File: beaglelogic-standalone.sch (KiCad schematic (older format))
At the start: 238 parts, among them J1 USB_OTG, J2 USB_A, J3 CONN_01X06, J4 SI-51009-F, J5 CONN_02X12, J6 CONN_02X16, Q1 BSS138, Q2 BSS138, SW1 SW_PUSH_SMALL_H, SW2 SW_PUSH_SMALL_H, U1 AP1117, U10 MCP79410/TDFN, U11 SST26VF064B, U12 TPS73101, U13 SN74LVCH16T245, U14 DVIULC6-4SC6, U15 DVIULC6-4SC6, U16 DVIULC6-4SC6, U17 DVIULC6-4SC6, U18 74LV1T125, U19 74LVC1G06, U2 TPS2051C, U20 EMMC_4G, U3 74LVC1G07, U4 TPD4S012, U5 TPD4S012, U6 OSD3358, U7 KSZ9031RNXCC, U8 74LVC2G241, U9 24LC32AT-I/OT, Y1 25MHz, Y2 24MHz, Y3 32.768kHz,CL=9pF

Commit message: Fix connection to GND of C31
Was unconnected though appeared connected

Signed-off-by: Kumar Abhishek <abhishek@theembeddedkitchen.net>
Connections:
- net GND: now also C31.2
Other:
- note added: "Serial Debug"

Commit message: Attach GPIO_OE to its own GPIO instead of SYS_RESETn
Signed-off-by: Kumar Abhishek <abhishek@theembeddedkitchen.net>
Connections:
- net SYS_RESETn: no longer R46.1
- net GPIO_OE: now reaches U6.T16 (GPMC_A10)
- net GPIO_OE: now also R46.1

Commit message: Add jumpered buffer to CS line of SPI Flash
Suggested change by @mwelling to enable recovery from a board brick.

Signed-off-by: Kumar Abhishek <abhishek@theembeddedkitchen.net>
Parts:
- added JP?: SPIF_Enable, Measurement_Points:Test_Point_2Pads, symbol Jumper_NC_Small
- added R?: 10K, Resistors_SMD:R_0402, symbol R
- added R?: 100K, Resistors_SMD:R_0402, symbol R
- U19: value 74LVC1G06 -> 74LVC1G125; symbol 74LVC1G06 -> 74LVC1G125
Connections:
- net +3V3: now also R?.2, R?.2
- net EMMC_RSTn: no longer U19.4
- net GND: now also JP?.1
- net SPIF_CS: now also U19.2; no longer U11.1 (S#)
- net EMMC_RESET renamed EMMC_RESETn
- net EMMC_RESETn: no longer U19.2
- new net: JP?.2, R?.1, U19.1
- new net: R?.1, U11.1 (S#), U19.4
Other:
- moved on the sheet: BT1, C53, U19

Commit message: Insert series resistors on SPIF SCK, eMMC CLK and SD CLK
Signed-off-by: Kumar Abhishek <abhishek@theembeddedkitchen.net>
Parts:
- added R? (x3): 33R, Resistors_SMD:R_0402, symbol R
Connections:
- net EMMC_CLK: now also R?.1; no longer R77.1, U20.M6 (CLK)
- net MMC0_CLK: now also R?.1; no longer R54.1, SOK1.5 (CLK)
- net SPIF_SCK: now also R?.1; no longer U11.6 (C)
- new net: R54.1, R?.2, SOK1.5 (CLK)
- new net: R77.1, R?.2, U20.M6 (CLK)
- new net: R?.2, U11.6 (C)
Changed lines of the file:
@@
 Text Label 17950 1700 2    50   ~ 0
 MMC0_CMD
-Text Label 17950 1900 2    50   ~ 0
+Text Label 16450 2700 2    50   ~ 0
 MMC0_CLK
 Text Label 17700 2100 2    50   ~ 0
@@
 Text Label 20850 2400 2    50   ~ 0
 EMMC_CMD
-Text Label 20850 2500 2    50   ~ 0
+Text Label 19950 2850 2    50   ~ 0
 EMMC_CLK
 $Comp
@@
 	0    -1   -1   0
 $EndComp
-Text Label 13900 2400 2    50   ~ 0
+Text Label 13500 2200 0    50   ~ 0
 SPIF_SCK
 Text Label 13900 2300 2    50   ~ 0
@@
 	16900 5700 17000 5700
 Wire Wire Line
-	17000 5700 17000 8000
+	17000 8000 17000 5700
 Wire Wire Line
-	17000 8000 16950 8000
+	16900 8000 16950 8000
 Wire Wire Line
-	16950 8000 16900 8000
+	16950 8000 17000 8000
 Wire Wire Line
 	16900 6000 17100 6000
@@
 	17050 1400 17050 1900
 Wire Wire Line
+	17050 1900 17050 2700
+Wire Wire Line
 	16850 1400 16850 2100
 Wire Wire Line
@@
 	19700 1350 19700 2500
 Wire Wire Line
-	19700 2500 20900 2500
+	19700 2500 20450 2500
+Wire Wire Line
+	20450 2500 20900 2500
 Wire Wire Line
 	19600 1350 19600 2650
@@
 Connection ~ 12950 2450
 Wire Wire Line
-	12400 2450 12250 2450
-Wire Wire Line
-	12250 2450 12250 2450
+	12250 2450 12400 2450
 $Comp
 L GND #PWR?
@@
 	0    1    1    0
 $EndComp
+$Comp
+L R R?
+U 1 1 596EAD95
+P 16800 2700
+F 0 "R?" V 16750 2950 50  0000 R CNN
+F 1 "33R" V 16800 2800 50  0000 R CNN
+F 2 "Resistors_SMD:R_0402" V 16730 2700 50  0001 C CNN
+F 3 "" H 16800 2700 50  0001 C CNN
+	1    16800 2700
+	0    -1   1    0
+$EndComp
+Wire Wire Line
+	17050 2700 16950 2700
+Connection ~ 17050 1900
+Wire Wire Line
+	16450 2700 16650 2700
+$Comp
+L R R?
+U 1 1 596ECB19
+P 20250 2850
+F 0 "R?" V 20200 3100 50  0000 R CNN
+F 1 "33R" V 20250 2950 50  0000 R CNN
+F 2 "Resistors_SMD:R_0402" V 20180 2850 50  0001 C CNN
+F 3 "" H 20250 2850 50  0001 C CNN
+	1    20250 2850
+	0    -1   1    0
+$EndComp
+Wire Wire Line
+	20400 2850 20450 2850
+Wire Wire Line
+	20450 2850 20450 2500
+Connection ~ 20450 2500
+Wire Wire Line
+	19950 2850 20100 2850
+$Comp
+L R R?
+U 1 1 596F921B
+P 13750 2400
+F 0 "R?" V 13700 2650 50  0000 R CNN
+F 1 "33R" V 13750 2500 50  0000 R CNN
+F 2 "Resistors_SMD:R_0402" V 13680 2400 50  0001 C CNN
+F 3 "" H 13750 2400 50  0001 C CNN
+	1    13750 2400
+	0    -1   1    0
+$EndComp
+Wire Wire Line
+	13600 2400 13450 2400
+Wire Wire Line
+	13450 2400 13450 2200
+Wire Wire Line
+	13450 2200 13500 2200
 $EndSCHEMATC

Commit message: Update to Revision A2
Signed-off-by: Kumar Abhishek <abhishek@theembeddedkitchen.net>
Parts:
- gave numbers to parts that had none: 6
- renumbered C53 to C37, C37 to C38, C38 to C39, C39 to C40, C40 to C41, C41 to C42, C42 to C43, C43 to C44, C44 to C45, C45 to C46, C46 to C47, C47 to C48, C48 to C49, C49 to C50, C50 to C51, C51 to C52, C52 to C53, R95 to R100, R96 to R101, R97 to R102, R98 to R103, R99 to R104, R100 to R105, R101 to R106, R102 to R107, R103 to R108, R104 to R109, R105 to R110, R106 to R111, R107 to R112, R108 to R113, R109 to R114, R110 to R115, R111 to R116, R112 to R117, R113 to R118, R114 to R119, R115 to R120, R116 to R121, R117 to R122, R118 to R123, R119 to R124, R42 to R45, R43 to R46, R44 to R47, R45 to R48, R46 to R49, R47 to R50, R48 to R51, R49 to R52, R50 to R53, R51 to R55, R52 to R56, R53 to R57, R54 to R58, R55 to R59, R56 to R60, R57 to R61, R58 to R62, R59 to R63, R60 to R64, R61 to R65, R62 to R66, R63 to R67, R64 to R68, R65 to R69, R66 to R70, R67 to R71, R68 to R72, R69 to R73, R70 to R74, R71 to R75, R72 to R76, R73 to R77, R74 to R78, R75 to R79, R76 to R80, R77 to R81, R78 to R82, R79 to R83, R80 to R84, R81 to R85, R82 to R86, R83 to R87, R84 to R88, R85 to R89, R86 to R90, R87 to R91, R88 to R92, R89 to R93, R90 to R94, R91 to R95, R92 to R97, R93 to R98, R94 to R99, U19 to U10, U10 to U11, U11 to U12, U12 to U13, U13 to U14, U14 to U15, U15 to U16, U16 to U17, U17 to U18, U18 to U19

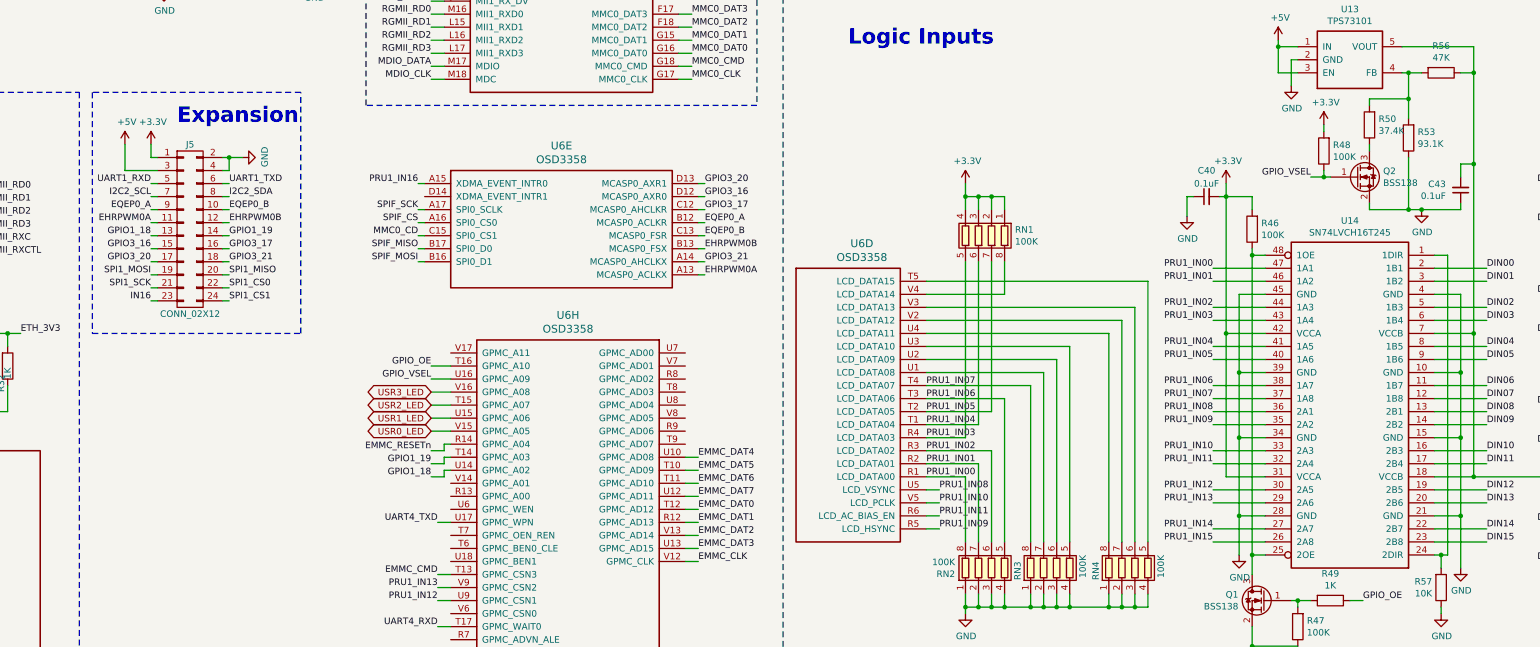
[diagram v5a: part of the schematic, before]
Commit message: Add pull-ups on I2C2 lines
Signed-off-by: Kumar Abhishek <abhishek@theembeddedkitchen.net>
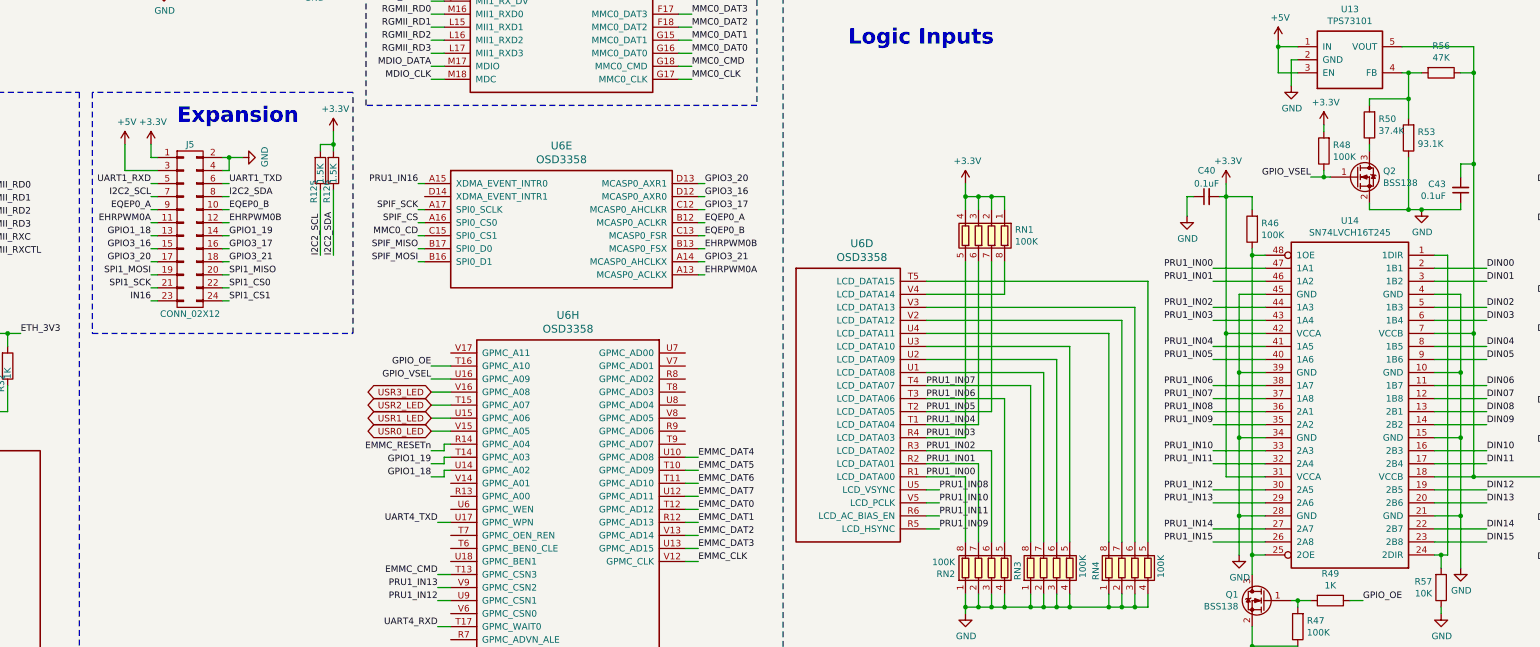
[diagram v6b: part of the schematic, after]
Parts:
- added R125, R126: 1.5K, Resistors_SMD:R_0402, symbol R
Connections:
- net +3V3: now also R125.2, R126.2
- net I2C2_SCL: now also R125.1
- net I2C2_SDA: now also R126.1

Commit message: Replace OSD3358 with OSD3358-SM
Signed-off-by: Kumar Abhishek <abhishek@theembeddedkitchen.net>
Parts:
- U6: value OSD3358 -> OSD3358-SM; symbol OSD3358 -> OSD3358-SM
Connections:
- net SPI_SCK is gone; now on net RGMII_TXC: U6.H16 (MII1_TX_CLK)
- net +3V3: now also U6.F6 (SYS_VDD1_3P3V_F6), U6.F7 (SYS_VDD1_3P3V_F7), U6.G6 (SYS_VDD1_3P3V_G6), U6.G7 (SYS_VDD1_3P3V_G7); no longer U6.U20 (SYS_VDD1_3P3V_U20), U6.V20 (SYS_VDD1_3P3V_V20)
- net +5V: now also U6.K6 (SYS_VOUT_K6), U6.K7 (SYS_VOUT_K7), U6.L6 (SYS_VOUT_L6), U6.L7 (SYS_VOUT_L7); no longer U6.W4 (SYS_VOUT_W4), U6.Y4 (SYS_VOUT_Y4)
- net 3P3_AUX: now also U6.F11 (SYS_VDD2_3P3V_F11), U6.G11 (SYS_VDD2_3P3V_G11); no longer U6.Y11 (SYS_VDD2_3P3V)
- net BAT_SENSE: now also U6.N7 (PMIC_BAT_SENSE); no longer U6.Y1 (BAT_VOLT)
- net EHRPWM0A: now also U6.A1 (MCASP0_ACLKX); no longer U6.A13 (MCASP0_ACLKX)
- net EHRPWM0B: now also U6.A2 (MCASP0_FSX); no longer U6.B13 (MCASP0_FSX)
- net EMMC_CLK: now also U6.T7 (GPMC_CLK); no longer U6.V12 (GPMC_CLK)
- net EMMC_CMD: now also U6.R7 (GPMC_CSN3); no longer U6.T13 (GPMC_CSN3)
- net EMMC_DAT0: now also U6.P6 (GPMC_AD12); no longer U6.T12 (GPMC_AD12)
- net EMMC_DAT1: now also U6.R6 (GPMC_AD13); no longer U6.R12 (GPMC_AD13)
- net EMMC_DAT2: now also U6.T6 (GPMC_AD14); no longer U6.V13 (GPMC_AD14)
- net EMMC_DAT3: now also U6.P7 (GPMC_AD15); no longer U6.U13 (GPMC_AD15)
- net EMMC_DAT4: now also U6.T4 (GPMC_AD8); no longer U6.U10 (GPMC_AD08)
- net EMMC_DAT5: now also U6.P5 (GPMC_AD9); no longer U6.T10 (GPMC_AD09)
- net EMMC_DAT6: now also U6.R5 (GPMC_AD10); no longer U6.T11 (GPMC_AD10)
- net EMMC_DAT7: now also U6.T5 (GPMC_AD11); no longer U6.U12 (GPMC_AD11)
- net EMMC_RESETn: now also U6.R13 (GPMC_A4); no longer U6.R14 (GPMC_A04)
- net EQEP0_A: now also U6.A3 (MCASP0_ACLKR); no longer U6.B12 (MCASP0_ACLKR)
- net EQEP0_B: now also U6.B3 (MCASP0_FSR); no longer U6.C13 (MCASP0_FSR)
- net GND: now also U6.D8 (DGND_D8), U6.D9 (DGND_D9), U6.E10 (DGND_E10), U6.E11 (DGND_E11), U6.E12 (DGND_E12), U6.E5 (DGND_E5), U6.E6 (DGND_E6), U6.E7 (DGND_E7), U6.E8 (DGND_E8), U6.E9 (DGND_E9), U6.F12 (DGND_F12), U6.F5 (DGND_F5), U6.G5 (DGND_G5), U6.H13 (DGND_H13), U6.H4 (DGND_H4), U6.H5 (DGND_H5), U6.J12 (DGND_J12), U6.J13 (DGND_J13), U6.J4 (DGND_J4), U6.J5 (DGND_J5), U6.K12 (DGND_K12), U6.K5 (DGND_K5), U6.L14 (USB1_ID), U6.L5 (DGND_L5), U6.M11 (DGND_M11), U6.M5 (DGND_M5), U6.N8 (DGND_N8), U6.N9 (DGND_N9); no longer U6.A1 (VSS_A1), U6.A18 (VSS_A18), U6.E19 (VSS_E19), U6.E20 (VSS_E20), U6.F19 (VSS_F19), U6.F8 (VSS_F8), U6.G11 (VSS_G11), U6.G19 (VSS_G19), U6.G8 (VSS_G8), U6.G9 (VSS_G9), U6.H10 (VSS_H10), U6.H19 (VSS_H19), U6.H6 (VSS_H6), U6.H7 (VSS_H7), U6.H8 (VSS_H8), U6.H9 (VSS_H9), U6.J10 (VSS_J10), U6.J11 (VSS_J11), U6.J19 (VSS_J19), U6.J20 (VSS_J20), U6.J6 (VSS_J6), U6.J7 (VSS_J7), U6.J8 (VSS_J8), U6.J9 (VSS_J9), U6.K10 (VSS_K10), U6.K11 (VSS_K11), U6.K19 (VSS_K19), U6.K7 (VSS_K7), U6.K9 (VSS_K9), U6.L10 (VSS_L10), U6.L11 (VSS_L11), U6.L13 (VSS_L13), U6.L19 (VSS_L19), U6.M14 (VSS_M14), U6.M19 (VSS_M19), U6.N10 (VSS_N10), U6.N11 (VSS_N11), U6.N14 (VSS_N14), U6.N19 (VSS_N19), U6.N20 (VSS_N20), U6.N7 (VSS_N7), U6.P17 (USB1_ID), U6.P19 (VSS_P19), U6.P20 (VSS_P20), U6.R19 (VSS_R19), U6.R20 (VSS_R20), U6.T19 (VSS_T19), U6.T20 (VSS_T20), U6.U19 (VSS_U19), U6.V1 (VSS_V1), U6.V18 (VSS_V18), U6.V19 (VSS_V19), U6.W10 (VSS_W10), U6.W11 (VSS_W11), U6.W12 (VSS_W12), U6.W13 (VSS_W13), U6.W14 (VSS_W14), U6.W15 (VSS_W15), U6.W16 (VSS_W16), U6.W17 (VSS_W17), U6.W18 (VSS_W18), U6.W19 (VSS_W19), U6.W2 (VSS_W2), U6.W20 (VSS_W20), U6.W3 (VSS_W3), U6.W5 (VSS_W5), U6.W6 (VSS_W6), U6.W7 (VSS_W7), U6.W8 (VSS_W8), U6.W9 (VSS_W9), U6.Y10 (VSS_Y10), U6.Y12 (VSS_Y12), U6.Y15 (VSS_Y15), U6.Y18 (VSS_Y18), U6.Y7 (VSS_Y7)
- net GPIO1_18: now also U6.P12 (GPMC_A2); no longer U6.U14 (GPMC_A02)
- net GPIO1_19: now also U6.T13 (GPMC_A3); no longer U6.T14 (GPMC_A03)
- net GPIO3_16: now also U6.B2 (MCASP0_AXR0); no longer U6.D12 (MCASP0_AXR0)
- net GPIO3_17: now also U6.B1 (MCASP0_AHCLKR); no longer U6.C12 (MCASP0_AHCLKR)
- net GPIO3_20: now also U6.C3 (MCASP0_AXR1); no longer U6.D13 (MCASP0_AXR1)
- net GPIO3_21: now also U6.C4 (MCASP0_AHCLKX); no longer U6.A14 (MCASP0_AHCLKX)
- net GPIO_OE: now also U6.R15 (GPMC_A10); no longer U6.T16 (GPMC_A10)
- net GPIO_VSEL: now also U6.T15 (GPMC_A9); no longer U6.U16 (GPMC_A09)
- net I2C0_SCL: now also U6.C10 (I2C0_SCL), U6.D10 (PMIC_SCL); no longer U6.C16 (I2C0_SCL), U6.C20 (PMIC_IN_I2C_SCL)
- net I2C0_SDA: now also U6.C11 (I2C0_SDA), U6.D11 (PMIC_SDA); no longer U6.C17 (I2C0_SDA), U6.C19 (PMIC_IN_I2C_SDA)
- net I2C2_SCL: now also U6.A10 (UART1_RTSN); no longer U6.D17 (UART1_RTSN)
- net I2C2_SDA: now also U6.B10 (UART1_CTSN); no longer U6.D18 (UART1_CTSN)
- net MDIO_CLK: now also U6.D13 (MDC); no longer U6.M18 (MDC)
- net MDIO_DATA: now also U6.E13 (MDIO); no longer U6.M17 (MDIO)
- net MMC0_CD: now also U6.C14 (SPI0_CS1); no longer U6.C15 (SPI0_CS1)
- net MMC0_CLK: now also U6.B15 (MMC0_CLK); no longer U6.G17 (MMC0_CLK)
- net MMC0_CMD: now also U6.B16 (MMC0_CMD); no longer U6.G18 (MMC0_CMD)
- net MMC0_DAT0: now also U6.A16 (MMC0_DAT0); no longer U6.G16 (MMC0_DAT0)
- net MMC0_DAT1: now also U6.A15 (MMC0_DAT1); no longer U6.G15 (MMC0_DAT1)
- net MMC0_DAT2: now also U6.C16 (MMC0_DAT2); no longer U6.F18 (MMC0_DAT2)
- net MMC0_DAT3: now also U6.C15 (MMC0_DAT3); no longer U6.F17 (MMC0_DAT3)
- net PMIC_PGOOD: now also U6.N12 (PMIC_PGOOD), U6.P11 (PWRONRSTN); no longer U6.A20 (PMIC_OUT_PGOOD), U6.B15 (PWRONRSTN)
- net PRU1_IN00: now also U6.G3 (LCD_DATA0); no longer U6.R1 (LCD_DATA00)
- net PRU1_IN01: now also U6.G2 (LCD_DATA1); no longer U6.R2 (LCD_DATA01)
- net PRU1_IN02: now also U6.G1 (LCD_DATA2); no longer U6.R3 (LCD_DATA02)
- net PRU1_IN03: now also U6.H3 (LCD_DATA3); no longer U6.R4 (LCD_DATA03)
- net PRU1_IN04: now also U6.H2 (LCD_DATA4); no longer U6.T1 (LCD_DATA04)
- net PRU1_IN05: now also U6.H1 (LCD_DATA5); no longer U6.T2 (LCD_DATA05)
- net PRU1_IN06: now also U6.J3 (LCD_DATA6); no longer U6.T3 (LCD_DATA06)
- net PRU1_IN07: now also U6.J2 (LCD_DATA7); no longer U6.T4 (LCD_DATA07)
- net PRU1_IN08: now also U6.F3 (LCD_VSYNC); no longer U6.U5 (LCD_VSYNC)
- net PRU1_IN09: now also U6.F2 (LCD_HSYNC); no longer U6.R5 (LCD_HSYNC)
- net PRU1_IN10: now also U6.F1 (LCD_PCLK); no longer U6.V5 (LCD_PCLK)
- net PRU1_IN11: now also U6.E1 (LCD_AC_BIAS_EN); no longer U6.R6 (LCD_AC_BIAS_EN)
- net PRU1_IN12: now also U6.P2 (GPMC_CSN1); no longer U6.U9 (GPMC_CSN1)
- net PRU1_IN13: now also U6.P1 (GPMC_CSN2); no longer U6.V9 (GPMC_CSN2)
- net PRU1_IN14: now also U6.A12 (UART0_RXD); no longer U6.E15 (UART0_RXD)
- net PRU1_IN15: now also U6.B12 (UART0_TXD); no longer U6.E16 (UART0_TXD)
- net PRU1_IN16: now also U6.A4 (XDMA_EVENT_INTR0); no longer U6.A15 (XDMA_EVENT_INTR0)
- net RGMII_RD0: now also U6.E14 (MII1_RXD0); no longer U6.M16 (MII1_RXD0)
- net RGMII_RD1: now also U6.D16 (MII1_RXD1); no longer U6.L15 (MII1_RXD1)
- net RGMII_RD2: now also U6.D15 (MII1_RXD2); no longer U6.L16 (MII1_RXD2)
- net RGMII_RD3: now also U6.D14 (MII1_RXD3); no longer U6.L17 (MII1_RXD3)
- net RGMII_RXC: now also U6.E16 (MII1_RX_CLK); no longer U6.L18 (MII1_RX_CLK)
- net RGMII_RXCTL: now also U6.F16 (MII1_RX_DV); no longer U6.J17 (MII1_RX_DV)
- net RGMII_TD0: now also U6.H15 (MII1_TXD0); no longer U6.K17 (MII1_TXD0)
- net RGMII_TD1: now also U6.H14 (MII1_TXD1); no longer U6.K16 (MII1_TXD1)
- net RGMII_TD2: now also U6.G16 (MII1_TXD2); no longer U6.K15 (MII1_TXD2)
- net RGMII_TD3: now also U6.G15 (MII1_TXD3); no longer U6.J18 (MII1_TXD3)
- net RGMII_TXC: no longer U6.K18 (MII1_TX_CLK)
- net RGMII_TXCTL: now also U6.G14 (MII1_TX_EN); no longer U6.J16 (MII1_TX_EN)
- net SPI1_CS0: now also U6.J14 (RMII1_REF_CLK); no longer U6.H18 (RMII1_REF_CLK)
- net SPI1_CS1: now also U6.C5 (ECAP0_IN_PWM0_OUT); no longer U6.C18 (ECAP0_IN_PWM0_OUT)
- net SPI1_MISO: now also U6.F14 (MII1_CRS); no longer U6.H17 (MII1_CRS)
- net SPI1_MOSI: now also U6.E15 (MII1_RX_ER); no longer U6.J15 (MII1_RX_ER)
- net SPI1_SCK: now also U6.F15 (MII1_COL)
- net SPIF_CS: now also U6.A14 (SPI0_CS0); no longer U6.A16 (SPI0_CS0)
- net SPIF_MISO: now also U6.B13 (SPI0_D0); no longer U6.B17 (SPI0_D0)
- net SPIF_MOSI: now also U6.B14 (SPI0_D1); no longer U6.B16 (SPI0_D1)
- net SPIF_SCK: now also U6.A13 (SPI0_SCLK); no longer U6.A17 (SPI0_SCLK)
- net SYS_RESETn: now also U6.R11 (WARMRSTN); no longer U6.A10 (WARMRSTN)
- net TS: now also U6.N6 (PMIC_TS); no longer U6.W1 (BAT_TEMP)
- net UART1_RXD: now also U6.A11 (UART1_RXD); no longer U6.D16 (UART1_RXD)
- net UART1_TXD: now also U6.B11 (UART1_TXD); no longer U6.D15 (UART1_TXD)
- net UART4_RXD: now also U6.P15 (GPMC_WAIT0); no longer U6.T17 (GPMC_WAIT0)
- net UART4_TXD: now also U6.R16 (GPMC_WPN); no longer U6.U17 (GPMC_WPN)
- net USB0_DM: now also U6.K16 (USB0_DM); no longer U6.N18 (USB0_DM)
- net USB0_DP: now also U6.K15 (USB0_DP); no longer U6.N17 (USB0_DP)
- net USB0_ID: now also U6.K14 (USB0_ID); no longer U6.P16 (USB0_ID)
- net USB0_VBUS: now also U6.J16 (USB0_VBUS), U6.P9 (VIN_USB_P9), U6.R9 (VIN_USB_R9), U6.T9 (VIN_USB_T9); no longer U6.P15 (USB0_VBUS), U6.Y8 (VIN_USB_Y8), U6.Y9 (VIN_USB_Y9)
- net USB1_DM: now also U6.L16 (USB1_DM); no longer U6.R18 (USB1_DM)
- net USB1_DP: now also U6.L15 (USB1_DP); no longer U6.R17 (USB1_DP)
- net USB1_DRVVBUS: now also U6.M14 (USB1_DRVVBUS); no longer U6.F15 (USB1_DRVVBUS)
- net USB1_VBUS: now also U6.M15 (USB1_VBUS); no longer U6.T18 (USB1_VBUS)
- net USR0_LED: now also U6.P13 (GPMC_A5); no longer U6.V15 (GPMC_A05)
- net USR1_LED: now also U6.T14 (GPMC_A6); no longer U6.U15 (GPMC_A06)
- net USR2_LED: now also U6.R14 (GPMC_A7); no longer U6.T15 (GPMC_A07)
- net USR3_LED: now also U6.P14 (GPMC_A8); no longer U6.V16 (GPMC_A08)
- net VBAT: now also U6.P8 (VIN_BAT_P8), U6.R8 (VIN_BAT_R8), U6.T8 (VIN_BAT_T8); no longer U6.Y2 (VIN_BAT_Y2), U6.Y3 (VIN_BAT_Y3)
- net VCC: now also U6.K11 (SYS_RTC_1P8V_K11), U6.L11 (SYS_RTC_1P8V_L11); no longer U6.E14 (SYS_RTC_1P8V_E14)
- net VDD_1V8: now also U6.K10 (SYS_VDD_1P8V_K10), U6.L10 (SYS_VDD_1P8V_L10); no longer U6.E9 (SYS_VDD_1P8V_E9), U6.R16 (SYS_VDD_1P8V_R16)
- net at R6.2: now also U6.M16 (RTC_KALDO_ENN); no longer U6.B4 (RTC_KALDO_ENN)
- net at SW2.2: now also U6.T11 (PMIC_PB_IN); no longer U6.D20 (PMIC_IN_PB_IN)
- net at C33.1, R38.1, Y2.2: now also U6.N16 (OSC0_OUT); no longer U6.K20 (OSC0_OUT)
- net at C32.2, C33.2: now also U6.N15 (OSC0_GND); no longer U6.L20 (OSC0_GND)
- net at C32.1, R38.2, Y2.1: now also U6.P16 (OSC0_IN); no longer U6.M20 (OSC0_IN)
- net at RN4.5 (R4.2): now also U6.M3 (LCD_DATA15); no longer U6.T5 (LCD_DATA15)
- net at RN3.7 (R2.2): now also U6.J1 (LCD_DATA8); no longer U6.U1 (LCD_DATA08)
- net at RN3.6 (R3.2): now also U6.K3 (LCD_DATA9); no longer U6.U2 (LCD_DATA09)
- net at RN3.5 (R4.2): now also U6.K2 (LCD_DATA10); no longer U6.U3 (LCD_DATA10)
- net at RN4.8 (R1.2): now also U6.K1 (LCD_DATA11); no longer U6.U4 (LCD_DATA11)
- net at RN4.7 (R2.2): now also U6.L3 (LCD_DATA12); no longer U6.V2 (LCD_DATA12)
- net at RN4.6 (R3.2): now also U6.L2 (LCD_DATA13); no longer U6.V3 (LCD_DATA13)
- net at RN1.8 (R1.2): now also U6.L1 (LCD_DATA14); no longer U6.V4 (LCD_DATA14)
- net VDDSHV: now reaches U6.L9 (VDDSHV3)
- net VDDSHV: now also U6.F8 (SYS_VDD3_3P3V_F8), U6.F9 (VDDSHV4), U6.G8 (SYS_VDD3_3P3V_G8), U6.G9 (VDDSHV5), U6.H7 (SYS_VDD3_3P3V_H7), U6.H8 (SYS_VDD3_3P3V_H8), U6.H9 (VDDSHV6), U6.J7 (SYS_VDD3_3P3V_J7), U6.J8 (SYS_VDD3_3P3V_J8), U6.J9 (VDDSHV1), U6.K8 (SYS_VDD3_3P3V_K8), U6.K9 (VDDSHV2), U6.L8 (SYS_VDD3_3P3V_L8)
- new net: U6.D4 (EXTINTN), U6.E4 (PMIC_NINT)
- new net: U6.L4 (PMIC_NWAKEUP), U6.M4 (EXT_WAKEUP)
- new net: U6.N10 (PMIC_POWER_EN), U6.N11 (PMIC_PWR_EN)
- new net: U6.N4 (PMIC_LDO_PGOOD), U6.N5 (RTC_PWRONRSTN)
- new net: TP1.1, U6.P10 (VIN_AC_P10), U6.R10 (VIN_AC_R10), U6.T10 (VIN_AC_T10)
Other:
- moved on the sheet: C12, C20, R3, R6, SW1, SW2, TP1, TP2, TP3, U3, U6B

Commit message: Convert to OSD3358-SM: Add missing pins, remove external EEPROM
Signed-off-by: Kumar Abhishek <abhishek@theembeddedkitchen.net>
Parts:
- removed C34: 0.1uF, Capacitors_SMD:C_0402, symbol C_Small
- removed R39: 1.5K, Resistors_SMD:R_0402, symbol R
- removed U9: 24LC32AT-I/OT, TO_SOT_Packages_SMD:SOT-23-5, symbol 24LC32AT-I/OT
- added J2: CONN_02X02, symbol CONN_02X02
- added R33: 1.5K, Resistors_SMD:R_0402, symbol R
- added TP6: I2C0_SCL, Measurement_Points:Measurement_Point_Round-SMD-Pad_Small, symbol TEST_1P
- added TP7: I2C0_SDA, Measurement_Points:Measurement_Point_Round-SMD-Pad_Small, symbol TEST_1P
- R41: value 1.5K -> 4.87K
- renumbered C12 to C10, C10 to C11, C11 to C12, C20 to C17, C17 to C18, C18 to C19, C19 to C20, C35 to C34, C36 to C35, C37 to C36, C38 to C37, C39 to C38, C40 to C39, C41 to C40, C42 to C41, C43 to C42, C44 to C43, C45 to C44, C46 to C45, C47 to C46, C48 to C47, C49 to C48, C50 to C49, C51 to C50, C52 to C51, C53 to C52, C54 to C53, C55 to C54, C56 to C55, C57 to C56, C58 to C57, C59 to C58, C60 to C59, C61 to C60, C62 to C61, C63 to C62, C64 to C63, C65 to C64, J2 to J3, J3 to J4, J4 to J5, J5 to J6, J6 to J7, R98 to R100, R99 to R101, R100 to R102, R101 to R103, R102 to R104, R103 to R105, R104 to R106, R105 to R107, R106 to R108, R107 to R109, R108 to R110, R109 to R111, R110 to R112, R111 to R113, R112 to R114, R113 to R115, R114 to R116, R115 to R117, R116 to R118, R117 to R119, R118 to R120, R119 to R121, R120 to R122, R121 to R123, R122 to R124, R123 to R125, R124 to R126, R33 to R34, R34 to R35, R35 to R36, R36 to R37, R37 to R38, R38 to R39, R125 to R42, R126 to R43, R42 to R44, R43 to R45, R44 to R46, R45 to R47, R46 to R48, R47 to R49, R48 to R50, R49 to R51, R50 to R52, R51 to R53, R52 to R54, R53 to R55, R54 to R56, R55 to R57, R56 to R58, R57 to R59, R58 to R60, R59 to R61, R60 to R62, R61 to R63, R62 to R64, R63 to R65, R64 to R66, R65 to R67, R66 to R68, R67 to R69, R68 to R70, R69 to R71, R70 to R72, R71 to R73, R72 to R74, R73 to R75, R74 to R76, R75 to R77, R76 to R78, R77 to R79, R78 to R80, R79 to R81, R80 to R82, R81 to R83, R82 to R84, R83 to R85, R84 to R86, R85 to R87, R86 to R88, R87 to R89, R88 to R90, R89 to R91, R90 to R92, R91 to R93, R92 to R94, R93 to R95, R94 to R96, R95 to R97, R96 to R98, R97 to R99, U3 to U1, U11 to U10, U12 to U11, U13 to U12, U14 to U13, U15 to U14, U16 to U15, U17 to U16, U18 to U17, U19 to U18, U20 to U19, U1 to U2, U2 to U3, U10 to U9
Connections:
- net +3V3: now also R33.2; no longer R41.2
- net BAT_SENSE: now also J2.3 (P3)
- net GND: now also R41.1, J2.4 (P4)
- net I2C0_SCL: now also R33.1, TP6.1
- net I2C0_SDA: now also TP7.1
- net TS: now also J2.2 (P2)
- net VBAT: now also J2.1 (P1)
- net at U6.M2 (EEPROM_WP): now also TP4.1
- net TRSTn: now reaches U6.D3 (TRSTN)
- net TRSTn: now also R41.2
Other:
- moved on the sheet: TP4, TP5, U6B
